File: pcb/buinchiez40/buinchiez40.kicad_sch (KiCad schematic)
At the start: 88 parts, among them SW10 SW_Push, SW11 SW_Push, SW12 SW_Push, SW13 SW_Push, SW14 SW_Push, SW15 SW_Push, SW16 SW_Push, SW17 SW_Push, SW18 SW_Push, SW19 SW_Push, SW2 SW_Push, SW20 SW_Push, SW21 SW_Push, SW22 SW_Push, SW23 SW_Push, SW24 SW_Push, SW25 SW_Push, SW26 SW_Push, SW27 SW_Push, SW28 SW_Push, SW29 SW_Push, SW3 SW_Push, SW30 SW_Push, SW31 SW_Push, SW32 SW_Push, SW33 SW_Push, SW34 SW_Push, SW35 SW_Push, SW36 SW_Push, SW37 SW_Push, SW38 SW_Push, SW39 SW_Push, SW4 SW_Push, SW40 SW_Push, SW5 SW_Push, SW6 SW_Push, SW7 SW_Push, SW8 SW_Push, SW9 SW_Push

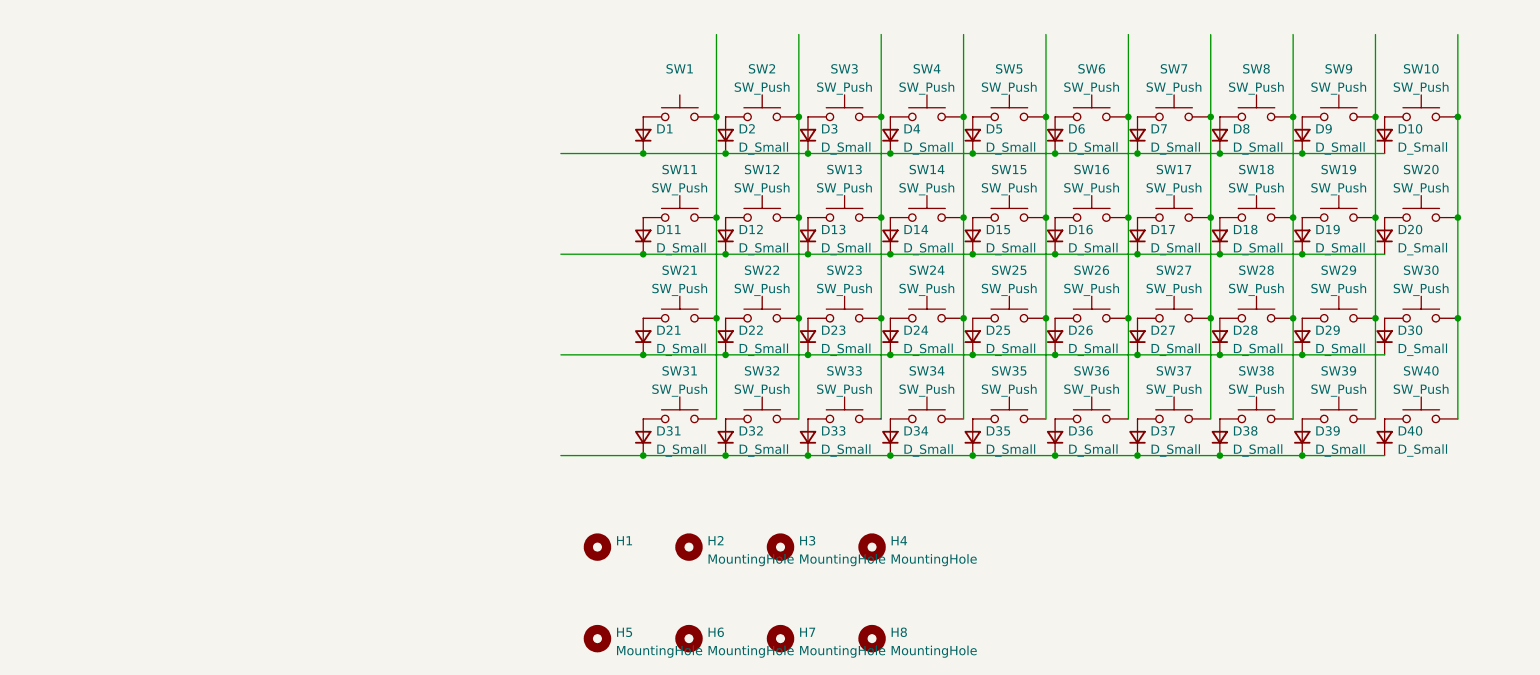
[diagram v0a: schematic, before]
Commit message: add pcb output and cases
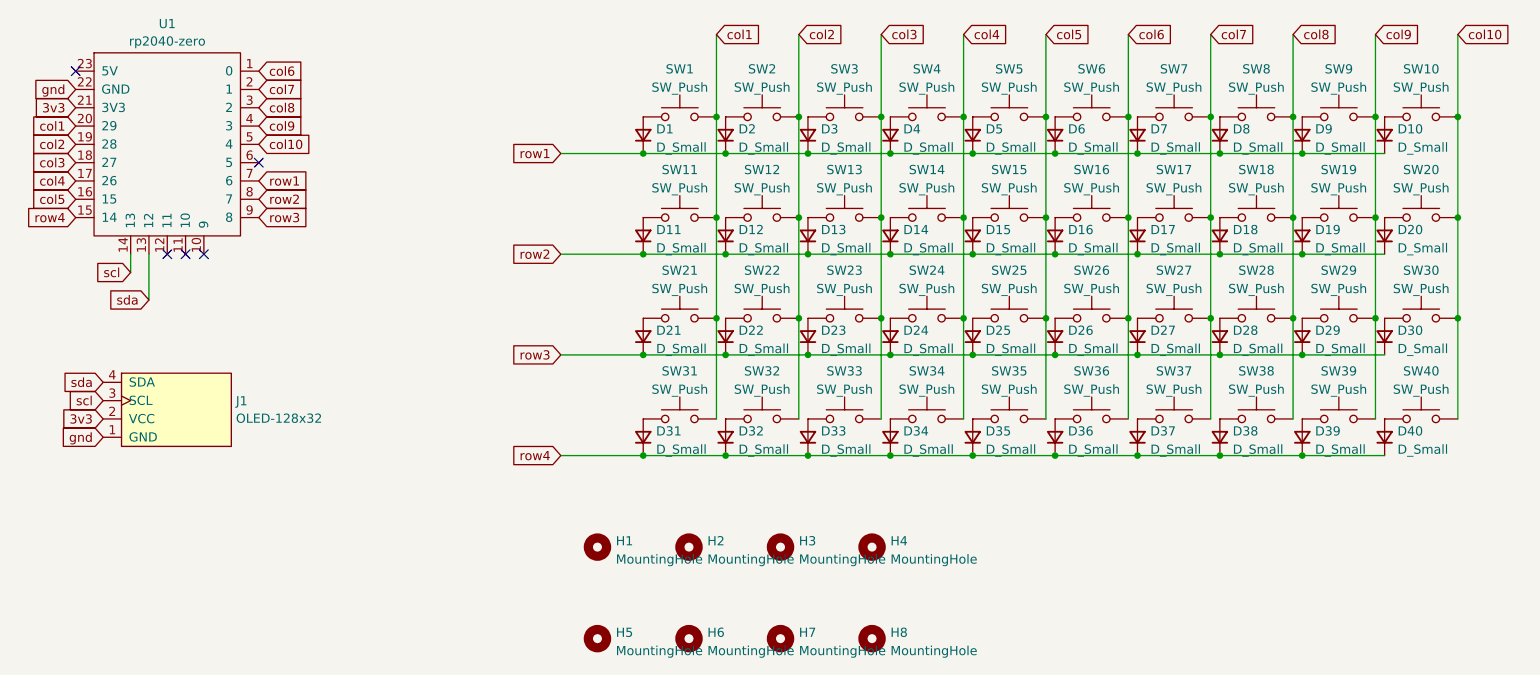
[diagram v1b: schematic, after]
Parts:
- added J1: OLED-128x32, display:OLED-128x32-cutout, symbol display:OLED-128x32
- added U1: rp2040-zero, mcu:rp2040-zero-tht, symbol mcu:rp2040-zero
- D1: value (none) -> D_Small; footprint (none) -> Diode_SMD:D_MiniMELF
- D10, D11, D12, D13, D14, D15, D16, D17, D18, D19, D2, D20, D21, D22, D23, D24, D25, D26, D27, D28, D29, D3, D30, D31, D32, D33, D34, D35, D36, D37, D38, D39, D4, D40, D5, D6, D7, D8, D9: footprint (none) -> Diode_SMD:D_MiniMELF
- H1: value (none) -> MountingHole; footprint (none) -> userlib:m1.6_hole
- H2, H3, H4, H5, H6, H7, H8: footprint (none) -> userlib:m1.6_hole
- SW1: value (none) -> SW_Push; footprint (none) -> userlib:Button_Mute_Kailh
- SW10, SW11, SW12, SW13, SW14, SW15, SW16, SW17, SW18, SW19, SW2, SW20, SW21, SW22, SW23, SW24, SW25, SW26, SW27, SW28, SW29, SW3, SW30, SW31, SW32, SW33, SW34, SW35, SW36, SW37, SW38, SW39, SW4, SW40, SW5, SW6, SW7, SW8, SW9: footprint (none) -> userlib:Button_Mute_Kailh
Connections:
- net col3: now reaches SW13.2, SW23.2, SW3.2, SW33.2
- net col3: now also U1.18 (27)
- net row4: now reaches D31.1 (K), D32.1 (K), D33.1 (K), D34.1 (K), D35.1 (K), D36.1 (K), D37.1 (K), D38.1 (K), D39.1 (K), D40.1 (K)
- net row4: now also U1.15 (14)
- net col1: now reaches SW1.2, SW11.2, SW21.2, SW31.2
- net col1: now also U1.20 (29)
- net row1: now reaches D1.1 (K), D10.1 (K), D2.1 (K), D3.1 (K), D4.1 (K), D5.1 (K), D6.1 (K), D7.1 (K), D8.1 (K), D9.1 (K)
- net row1: now also U1.7 (6)
- net row3: now reaches D21.1 (K), D22.1 (K), D23.1 (K), D24.1 (K), D25.1 (K), D26.1 (K), D27.1 (K), D28.1 (K), D29.1 (K), D30.1 (K)
- net row3: now also U1.9 (8)
- net row2: now reaches D11.1 (K), D12.1 (K), D13.1 (K), D14.1 (K), D15.1 (K), D16.1 (K), D17.1 (K), D18.1 (K), D19.1 (K), D20.1 (K)
- net row2: now also U1.8 (7)
- net col5: now reaches SW15.2, SW25.2, SW35.2, SW5.2
- net col5: now also U1.16 (15)
- net col10: now reaches SW10.2, SW20.2, SW30.2, SW40.2
- net col10: now also U1.5 (4)
- net col9: now reaches SW19.2, SW29.2, SW39.2, SW9.2
- net col9: now also U1.4 (3)
- net col7: now reaches SW17.2, SW27.2, SW37.2, SW7.2
- net col7: now also U1.2 (1)
- net col6: now reaches SW16.2, SW26.2, SW36.2, SW6.2
- net col6: now also U1.1 (0)
- net col8: now reaches SW18.2, SW28.2, SW38.2, SW8.2
- net col8: now also U1.3 (2)
- net col2: now reaches SW12.2, SW2.2, SW22.2, SW32.2
- net col2: now also U1.19 (28)
- net col4: now reaches SW14.2, SW24.2, SW34.2, SW4.2
- net col4: now also U1.17 (26)
- new net 3v3: J1.2 (VCC), U1.21 (3V3)
- new net gnd: J1.1 (GND), U1.22 (GND)
- new net scl: J1.3 (SCL), U1.14 (13)
- new net sda: J1.4 (SDA), U1.13 (12)
- no-connect marks 0 -> 5

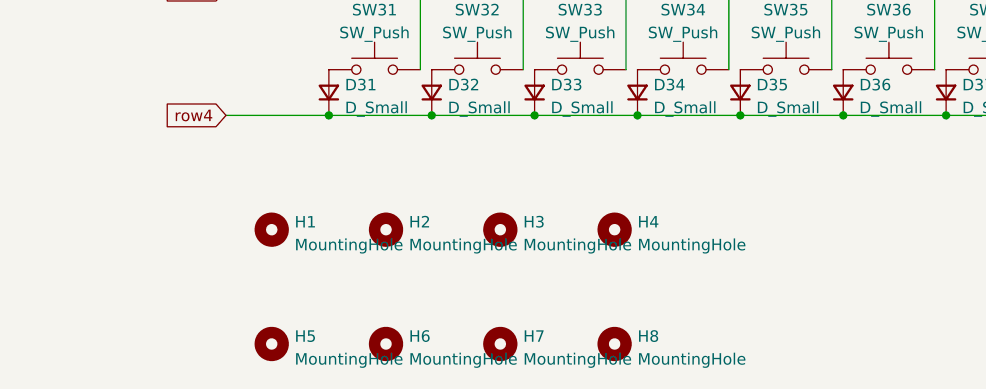
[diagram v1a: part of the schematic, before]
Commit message: add grounding pads
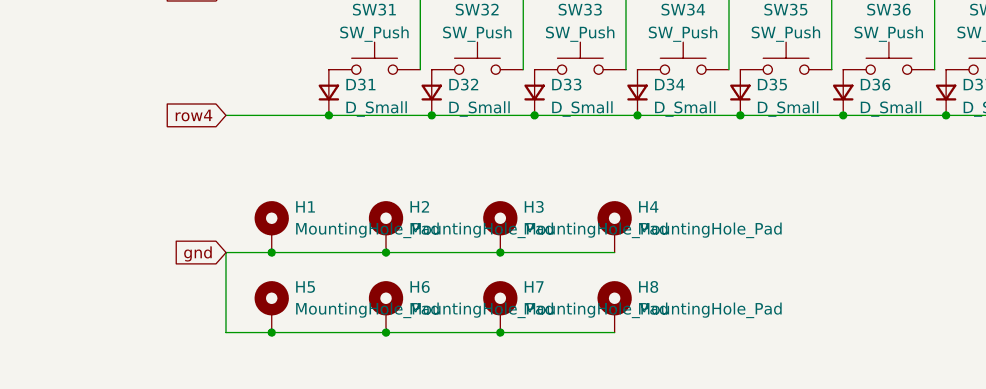
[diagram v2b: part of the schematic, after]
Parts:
- removed H1, H2, H3, H4, H5, H6, H7, H8: MountingHole, userlib:m1.6_hole, symbol Mechanical:MountingHole
- added H1, H2, H3, H4, H5, H6, H7, H8: MountingHole_Pad, userlib:m1.6_hole, symbol Mechanical:MountingHole_Pad
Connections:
- net gnd: now also H1.1, H2.1, H3.1, H4.1, H5.1, H6.1, H7.1, H8.1
